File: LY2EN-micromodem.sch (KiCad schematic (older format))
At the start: 19 parts, among them Q1 2N7000

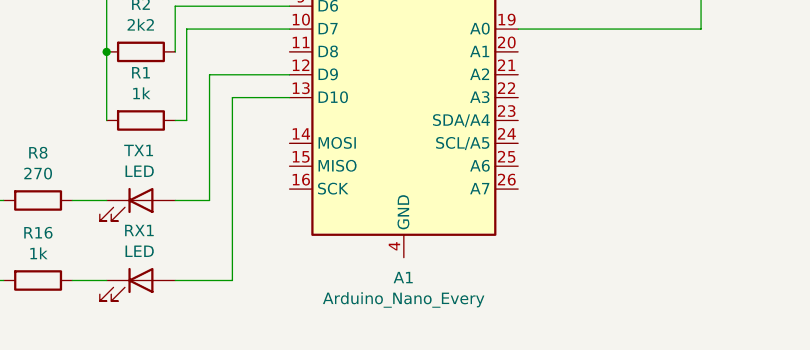
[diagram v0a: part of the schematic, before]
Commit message: Shrink SMD components down from 1812 to 0805
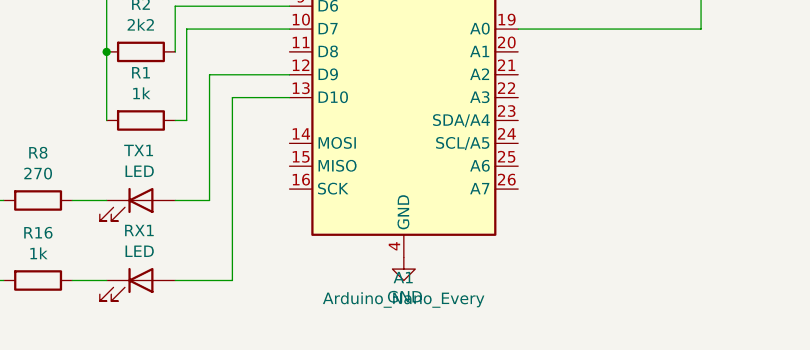
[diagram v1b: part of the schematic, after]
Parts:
- C1, C2, C3: footprint Capacitor_SMD:C_1812_4532Metric_Pad1.57x3.40mm_HandSolder -> Capacitor_SMD:C_0805_2012Metric_Pad1.18x1.45mm_HandSolder
- R1, R10, R11, R16, R2, R3, R4, R6, R7, R8, R9: footprint Resistor_SMD:R_1812_4532Metric_Pad1.30x3.40mm_HandSolder -> Resistor_SMD:R_0805_2012Metric_Pad1.20x1.40mm_HandSolder
- R5: footprint Potentiometer_SMD:Potentiometer_Vishay_TS53YL_Vertical -> Potentiometer_THT:Potentiometer_Bourns_3296W_Vertical
- RX1, TX1: footprint LED_SMD:LED_1812_4532Metric_Pad1.30x3.40mm_HandSolder -> LED_SMD:LED_0805_2012Metric_Pad1.15x1.40mm_HandSolder
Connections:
- net GND: now also A1.29 (GND), A1.4 (GND)
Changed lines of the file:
@@
 F 0 "C1" V 4348 3100 50  0000 C CNN
 F 1 "100nF" V 4439 3100 50  0000 C CNN
-F 2 "Capacitor_SMD:C_1812_4532Metric_Pad1.57x3.40mm_HandSolder" H 4638 2950 50  0001 C CNN
+F 2 "Capacitor_SMD:C_0805_2012Metric_Pad1.18x1.45mm_HandSolder" H 4638 2950 50  0001 C CNN
 F 3 "~" H 4600 3100 50  0001 C CNN
 	1    4600 3100
@@
 F 0 "R6" V 4807 2050 50  0000 C CNN
 F 1 "1k" V 4716 2050 50  0000 C CNN
-F 2 "Resistor_SMD:R_1812_4532Metric_Pad1.30x3.40mm_HandSolder" V 4530 2050 50  0001 C CNN
+F 2 "Resistor_SMD:R_0805_2012Metric_Pad1.20x1.40mm_HandSolder" V 4530 2050 50  0001 C CNN
 F 3 "~" H 4600 2050 50  0001 C CNN
 	1    4600 2050
@@
 F 0 "C2" H 5015 2896 50  0000 L CNN
 F 1 "4.7uF" H 5015 2805 50  0000 L CNN
-F 2 "Capacitor_SMD:C_1812_4532Metric_Pad1.57x3.40mm_HandSolder" H 4938 2700 50  0001 C CNN
+F 2 "Capacitor_SMD:C_0805_2012Metric_Pad1.18x1.45mm_HandSolder" H 4938 2700 50  0001 C CNN
 F 3 "~" H 4900 2850 50  0001 C CNN
 	1    4900 2850
@@
 F 0 "R7" V 4807 3450 50  0000 C CNN
 F 1 "270" V 4716 3450 50  0000 C CNN
-F 2 "Resistor_SMD:R_1812_4532Metric_Pad1.30x3.40mm_HandSolder" V 4530 3450 50  0001 C CNN
+F 2 "Resistor_SMD:R_0805_2012Metric_Pad1.20x1.40mm_HandSolder" V 4530 3450 50  0001 C CNN
 F 3 "~" H 4600 3450 50  0001 C CNN
 	1    4600 3450
@@
 F 0 "R5" H 4830 2354 50  0000 R CNN
 F 1 "100k" H 4830 2445 50  0000 R CNN
-F 2 "Potentiometer_SMD:Potentiometer_Vishay_TS53YL_Vertical" H 4900 2400 50  0001 C CNN
+F 2 "Potentiometer_THT:Potentiometer_Bourns_3296W_Vertical" H 4900 2400 50  0001 C CNN
 F 3 "~" H 4900 2400 50  0001 C CNN
 	1    4900 2400
@@
 F 0 "R4" V 4843 3700 50  0000 C CNN
 F 1 "8k2" V 4934 3700 50  0000 C CNN
-F 2 "Resistor_SMD:R_1812_4532Metric_Pad1.30x3.40mm_HandSolder" V 4980 3700 50  0001 C CNN
+F 2 "Resistor_SMD:R_0805_2012Metric_Pad1.20x1.40mm_HandSolder" V 4980 3700 50  0001 C CNN
 F 3 "~" H 5050 3700 50  0001 C CNN
 	1    5050 3700
@@
 F 0 "R3" V 4843 4000 50  0000 C CNN
 F 1 "3k9" V 4934 4000 50  0000 C CNN
-F 2 "Resistor_SMD:R_1812_4532Metric_Pad1.30x3.40mm_HandSolder" V 4980 4000 50  0001 C CNN
+F 2 "Resistor_SMD:R_0805_2012Metric_Pad1.20x1.40mm_HandSolder" V 4980 4000 50  0001 C CNN
 F 3 "~" H 5050 4000 50  0001 C CNN
 	1    5050 4000
@@
 F 0 "R2" V 4843 4300 50  0000 C CNN
 F 1 "2k2" V 4934 4300 50  0000 C CNN
-F 2 "Resistor_SMD:R_1812_4532Metric_Pad1.30x3.40mm_HandSolder" V 4980 4300 50  0001 C CNN
+F 2 "Resistor_SMD:R_0805_2012Metric_Pad1.20x1.40mm_HandSolder" V 4980 4300 50  0001 C CNN
 F 3 "~" H 5050 4300 50  0001 C CNN
 	1    5050 4300
@@
 F 0 "R1" V 4843 4600 50  0000 C CNN
 F 1 "1k" V 4934 4600 50  0000 C CNN
-F 2 "Resistor_SMD:R_1812_4532Metric_Pad1.30x3.40mm_HandSolder" V 4980 4600 50  0001 C CNN
+F 2 "Resistor_SMD:R_0805_2012Metric_Pad1.20x1.40mm_HandSolder" V 4980 4600 50  0001 C CNN
 F 3 "~" H 5050 4600 50  0001 C CNN
 	1    5050 4600
@@
 F 0 "C3" H 7385 3054 50  0000 R CNN
 F 1 "1uF" H 7385 3145 50  0000 R CNN
-F 2 "Capacitor_SMD:C_1812_4532Metric_Pad1.57x3.40mm_HandSolder" H 7538 2950 50  0001 C CNN
+F 2 "Capacitor_SMD:C_0805_2012Metric_Pad1.18x1.45mm_HandSolder" H 7538 2950 50  0001 C CNN
 F 3 "~" H 7500 3100 50  0001 C CNN
 	1    7500 3100
@@
 F 0 "R10" V 7643 4000 50  0000 C CNN
 F 1 "100k" V 7734 4000 50  0000 C CNN
-F 2 "Resistor_SMD:R_1812_4532Metric_Pad1.30x3.40mm_HandSolder" V 7780 4000 50  0001 C CNN
+F 2 "Resistor_SMD:R_0805_2012Metric_Pad1.20x1.40mm_HandSolder" V 7780 4000 50  0001 C CNN
 F 3 "~" H 7850 4000 50  0001 C CNN
 	1    7850 4000
@@
 F 0 "R11" V 6943 4000 50  0000 C CNN
 F 1 "100k" V 7034 4000 50  0000 C CNN
-F 2 "Resistor_SMD:R_1812_4532Metric_Pad1.30x3.40mm_HandSolder" V 7080 4000 50  0001 C CNN
+F 2 "Resistor_SMD:R_0805_2012Metric_Pad1.20x1.40mm_HandSolder" V 7080 4000 50  0001 C CNN
 F 3 "~" H 7150 4000 50  0001 C CNN
 	1    7150 4000
@@
 F 0 "R9" H 5780 2804 50  0000 R CNN
 F 1 "10k" H 5780 2895 50  0000 R CNN
-F 2 "Resistor_SMD:R_1812_4532Metric_Pad1.30x3.40mm_HandSolder" V 5780 2850 50  0001 C CNN
+F 2 "Resistor_SMD:R_0805_2012Metric_Pad1.20x1.40mm_HandSolder" V 5780 2850 50  0001 C CNN
 F 3 "~" H 5850 2850 50  0001 C CNN
 	1    5850 2850
@@
 F 0 "TX1" H 5043 5167 50  0000 C CNN
 F 1 "LED" H 5043 5076 50  0000 C CNN
-F 2 "LED_SMD:LED_1812_4532Metric_Pad1.30x3.40mm_HandSolder" H 5050 4950 50  0001 C CNN
+F 2 "LED_SMD:LED_0805_2012Metric_Pad1.15x1.40mm_HandSolder" H 5050 4950 50  0001 C CNN
 F 3 "~" H 5050 4950 50  0001 C CNN
 	1    5050 4950
@@
 F 0 "RX1" H 5043 5517 50  0000 C CNN
 F 1 "LED" H 5043 5426 50  0000 C CNN
-F 2 "LED_SMD:LED_1812_4532Metric_Pad1.30x3.40mm_HandSolder" H 5050 5300 50  0001 C CNN
+F 2 "LED_SMD:LED_0805_2012Metric_Pad1.15x1.40mm_HandSolder" H 5050 5300 50  0001 C CNN
 F 3 "~" H 5050 5300 50  0001 C CNN
 	1    5050 5300
@@
 F 0 "R8" V 4393 4950 50  0000 C CNN
 F 1 "270" V 4484 4950 50  0000 C CNN
-F 2 "Resistor_SMD:R_1812_4532Metric_Pad1.30x3.40mm_HandSolder" V 4530 4950 50  0001 C CNN
+F 2 "Resistor_SMD:R_0805_2012Metric_Pad1.20x1.40mm_HandSolder" V 4530 4950 50  0001 C CNN
 F 3 "~" H 4600 4950 50  0001 C CNN
 	1    4600 4950
@@
 F 0 "R16" V 4393 5300 50  0000 C CNN
 F 1 "1k" V 4484 5300 50  0000 C CNN
-F 2 "Resistor_SMD:R_1812_4532Metric_Pad1.30x3.40mm_HandSolder" V 4530 5300 50  0001 C CNN
+F 2 "Resistor_SMD:R_0805_2012Metric_Pad1.20x1.40mm_HandSolder" V 4530 5300 50  0001 C CNN
 F 3 "~" H 4600 5300 50  0001 C CNN
 	1    4600 5300
@@
 Connection ~ 6100 2850
 Connection ~ 4300 5300
+$Comp
+L power:GND #PWR?
+U 1 1 608BD52C
+P 6200 5200
+F 0 "#PWR?" H 6200 4950 50  0001 C CNN
+F 1 "GND" H 6205 5027 50  0000 C CNN
+F 2 "" H 6200 5200 50  0001 C CNN
+F 3 "" H 6200 5200 50  0001 C CNN
+	1    6200 5200
+	1    0    0    -1
+$EndComp
 $EndSCHEMATC
